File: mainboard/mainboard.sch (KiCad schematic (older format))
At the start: 29 parts, among them U1 ESP32-WROOM-32, U3 tps63070

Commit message: Add basic circuitry
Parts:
- added C12, C15, C18, C21, C24, C25, C3, C6, C9, C? (x10): C, symbol Device:C
- added C? (x2): 1 nC, symbol Device:C
- added D?: SP0503BAHT, Package_TO_SOT_SMD:SOT-143, symbol Power_Protection:SP0503BAHT
- added D?: D_Schottky, symbol Device:D_Schottky
- added J?: USB_B_Micro, symbol Connector:USB_B_Micro
- added J? (x2): Conn_01x19_MountingPin, symbol Connector_Generic_MountingPin:Conn_01x19_MountingPin
- added L3: L, symbol Device:L
- added Q?: PMV32UP, Package_TO_SOT_SMD:SOT-23, symbol pmv32up:PMV32UP
- added Q? (x2): Q_NPN_BCE, symbol Device:Q_NPN_BCE
- added R12, R13, R14, R3, R8, R9: R, symbol Device:R
- added R?: 4.7 kR, symbol Device:R
- added R? (x3): 470 R, symbol Device:R
- added R?: 100 kR, symbol Device:R
- added R?: 1 kR, symbol Device:R
- added R? (x2): 12 kR, symbol Device:R
- added SW? (x2): SW_Push, symbol Switch:SW_Push
- added U4: tps63070, tps63070:VQFN-HR-15, symbol tps63070:tps63070
- added U5: CP2102N-A01-GQFN24, Package_DFN_QFN:QFN-24-1EP_4x4mm_P0.5mm_EP2.6x2.6mm, symbol Interface_USB:CP2102N-A01-GQFN24
- gave numbers to parts that had none: 27
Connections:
- net labels added: D+, D-, DTR, EN, GSCLK, IO0, LAT, RTS, RXD, SCLK, SIN0, SOUT0, SOUT1, TXD, VBUS, VDC, VUSB, ~PG_VCC0, ~PG_VCC1
- net labels removed: +VDC, ~PG_VCC
- wire segments 144 -> 434
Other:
- note added: "balancing\nresistor"
- moved on the sheet: U1

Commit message: Add sensors
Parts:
- removed R13, R14: R, symbol Device:R
- added C?: 100 nC, Capacitor_SMD:C_0805_2012Metric, symbol Device:C
- added C?: 100 nC, symbol Device:C
- added C?: C, symbol Device:C
- added F? (x3): Fuse, symbol Device:Fuse
- added JP? (x2): Jumper_3_Bridged12, symbol Jumper:Jumper_3_Bridged12
- added U?: BME680, Package_LGA:Bosch_LGA-8_3x3mm_P0.8mm_ClockwisePinNumbering, symbol Sensor:BME680
- added U?: BH1750FVI, symbol BH1750:BH1750FVI
- C1, C16, C17, C18, C19, C2, C20, C21, C22, C23, C24, C25, C3, C4, C5, C6: footprint (none) -> Capacitor_SMD:C_0805_2012Metric
- C10, C11, C12: value C -> 100 nC; footprint (none) -> Capacitor_SMD:C_0805_2012Metric
- C13, C14, C15, C7, C8, C9: footprint (none) -> Capacitor_SMD:C_0603_1608Metric
- C26, C27, C28, C29, C30, C31, C32, C33, C34, C35, C36, C37: renamed from C?; footprint (none) -> Capacitor_SMD:C_0805_2012Metric
- J2, J3: renamed from J?; footprint (none) -> mainboard:Molex_Easy-On_52746-1971_1x19_P0.5mm_Horizontal
- L1, L2, L3: footprint (none) -> Inductor_SMD:L_Coilcraft_XxL4020
- R1, R10, R11, R12, R2, R3: value R -> 10 kR; footprint (none) -> Resistor_SMD:R_0805_2012Metric
- R15, R16, R17, R18, R19, R20, R21, R22: renamed from R?; footprint (none) -> Resistor_SMD:R_0805_2012Metric
- R4, R6, R8: value R -> 470 kR; footprint (none) -> Resistor_SMD:R_0805_2012Metric
- R5: value R -> 150 kR; footprint (none) -> Resistor_SMD:R_0805_2012Metric
- R7, R9: value R -> 120 kR; footprint (none) -> Resistor_SMD:R_0805_2012Metric
- gave numbers to parts that had none: 8
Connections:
- net labels added: PG_3V3, PG_VCC0, PG_VCC1, SCL, SDA, VCC_EAR0, VCC_EAR1
- net labels removed: VCC, ~PG_3V3, ~PG_VCC0, ~PG_VCC1
- wire segments 434 -> 478
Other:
- note added: "BOOT SELECT"
- note added: "EAR CONNECTORS"
- note added: "ENVIRON I2C"
- note added: "LED VCC"
- note added: "LUX I2C"
- note added: "POWER SELECT"
- note added: "USB <-> UART"
- note added: "VDD 3V3"
- note added: "WROOM32"
- note removed: "balancing\nresistor"
- moved on the sheet: C25, C26, C27, C28, C29, C30, C31, C32, C33, C34, C35, C36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

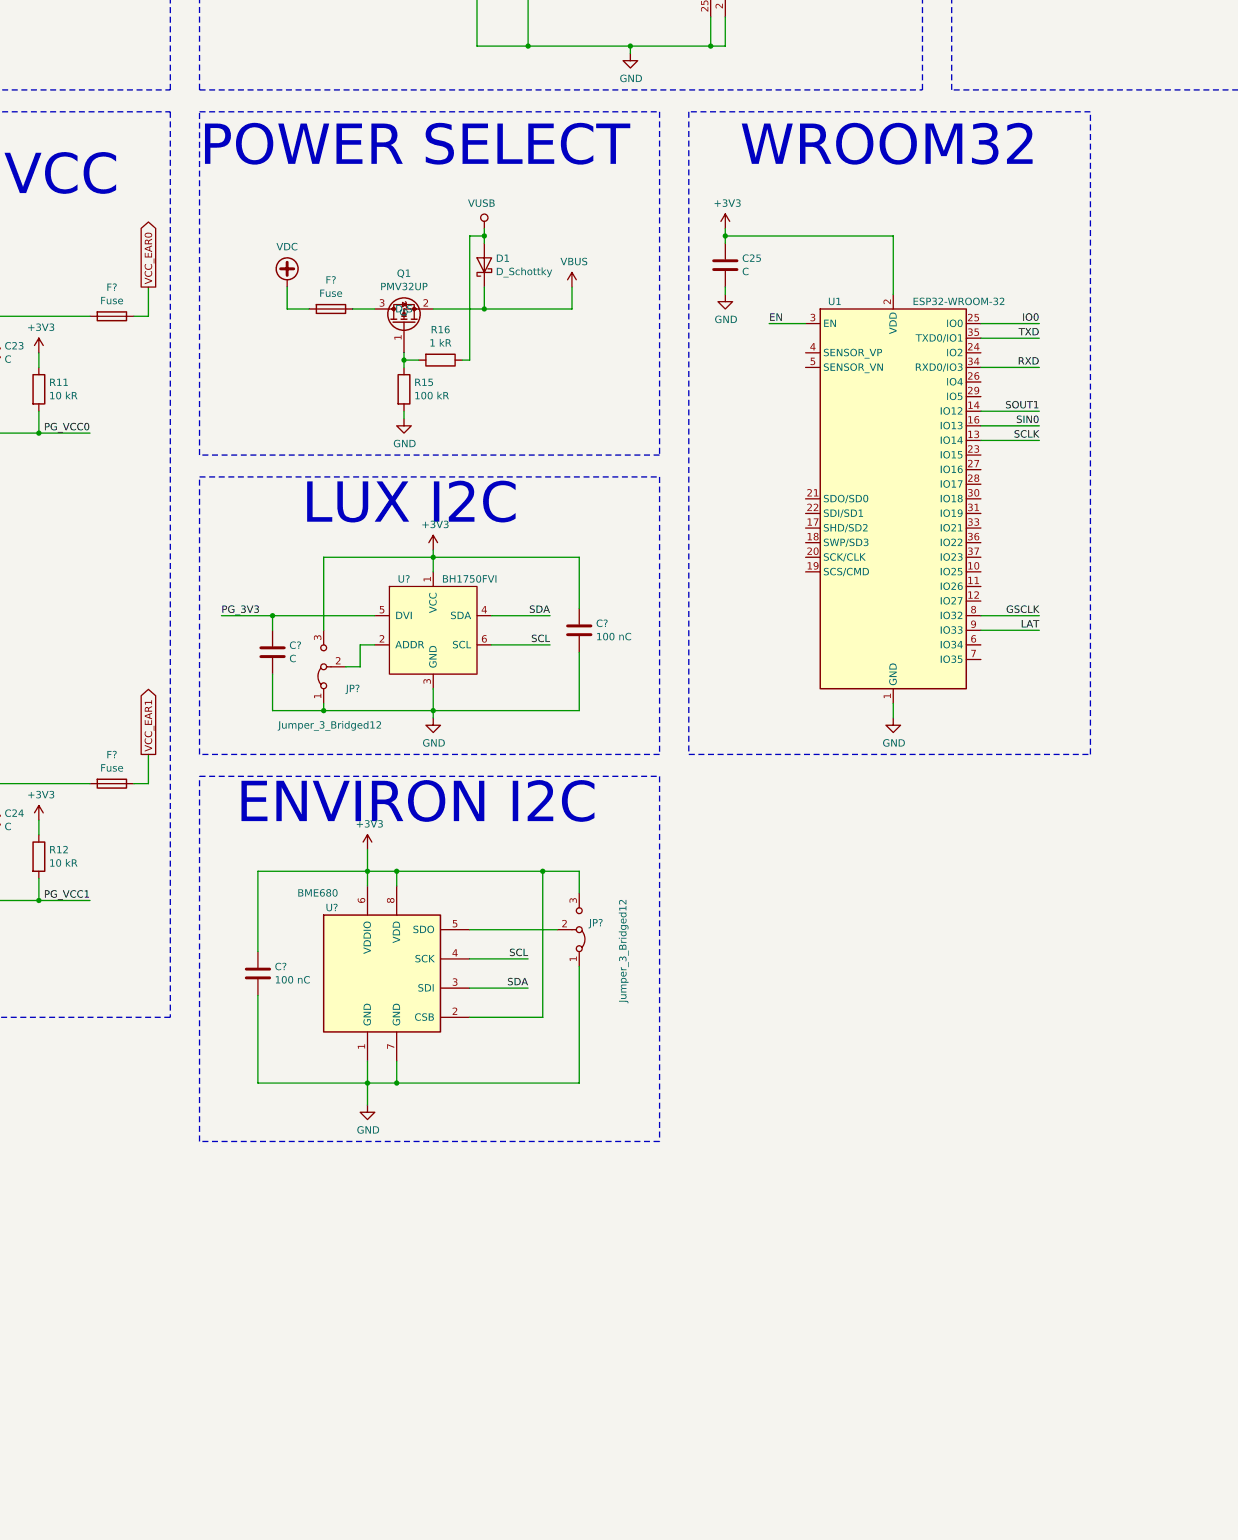
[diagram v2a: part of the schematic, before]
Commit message: Add accelerometer and magnetometer
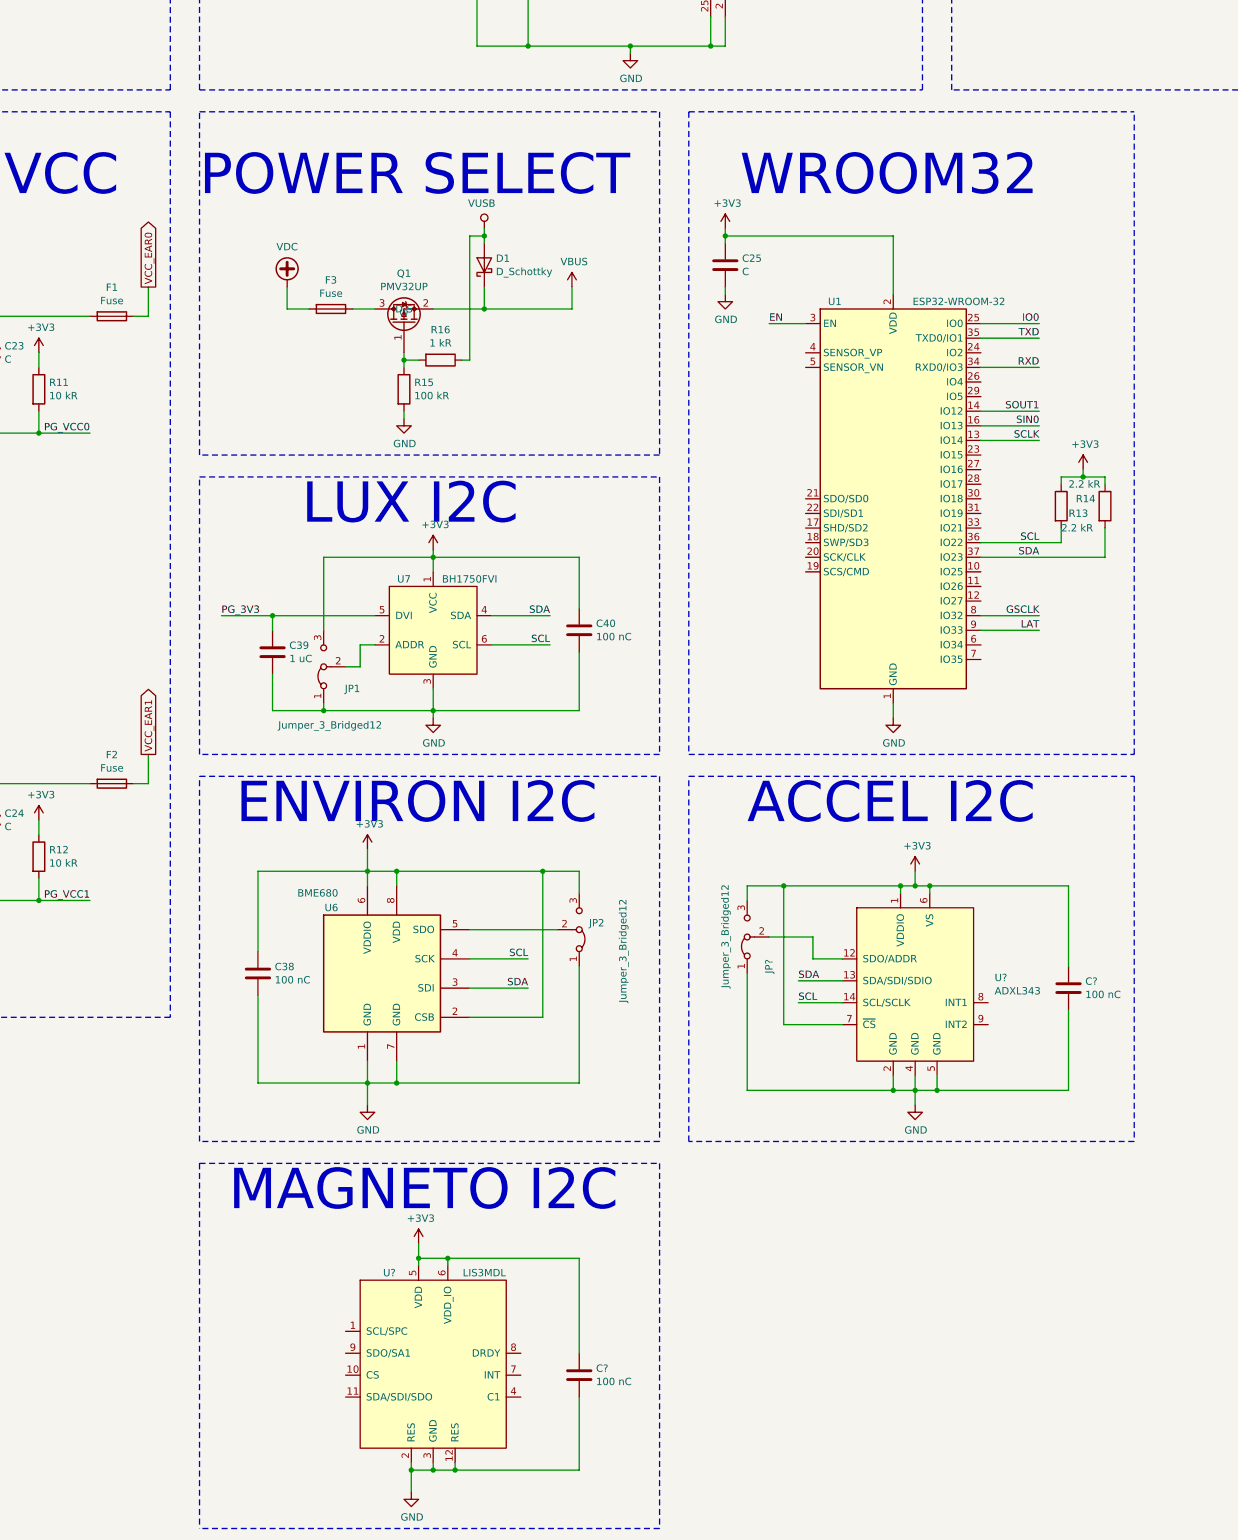
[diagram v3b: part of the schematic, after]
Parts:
- added C? (x2): 100 nC, symbol Device:C
- added JP?: Jumper_3_Bridged12, symbol Jumper:Jumper_3_Bridged12
- added R13, R14: 2.2 kR, symbol Device:R
- added U?: LIS3MDL, symbol LIS3MDL:LIS3MDL
- added U?: ADXL343, symbol ADXL343:ADXL343
- C39: renamed from C?; value C -> 1 uC
- gave numbers to parts that had none: 9
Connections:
- net +3V3: now also C?.1, C?.1, JP?.3 (B), R13.1, R14.1, U?.1 (VDDIO), U?.5 (VDD), U?.6 (VDD_IO), U?.6 (VS), U?.7 (~CS)
- net GND: now also C?.2, C?.2, JP?.1 (A), U?.12 (RES), U?.2 (GND), U?.2 (RES), U?.3 (GND), U?.4 (GND), U?.5 (GND)
- net SCL: now also U1.36 (IO22), R13.2, U?.14 (SCL/SCLK)
- net SDA: now also U1.37 (IO23), R14.2, U?.13 (SDA/SDI/SDIO)
- new net: JP?.2 (C), U?.12 (SDO/ADDR)
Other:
- note added: "ACCEL I2C"
- note added: "MAGNETO I2C"

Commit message: Layouting WIP
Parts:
- removed JP?: Jumper_3_Bridged12, symbol Jumper:Jumper_3_Bridged12
- removed Q1: PMV32UP, Package_TO_SOT_SMD:SOT-23, symbol pmv32up:PMV32UP
- removed Q2, Q3: Q_NPN_BCE, symbol Device:Q_NPN_BCE
- added C41: 100 nC, Capacitor_SMD:C_0805_2012Metric, symbol Device:C
- added JP3: Jumper_3_Bridged12, Jumper:SolderJumper-3_P1.3mm_Bridged12_Pad1.0x1.5mm, symbol Jumper:Jumper_3_Bridged12
- added JP4: Jumper, Jumper:SolderJumper-2_P1.3mm_Bridged_Pad1.0x1.5mm, symbol Device:Jumper
- added Q1: DMG2301L, Package_TO_SOT_SMD:SOT-23, symbol Transistor_FET:DMG2301L
- added Q2, Q3: MMBT3904, Package_TO_SOT_SMD:SOT-23, symbol Transistor_BJT:MMBT3904
- C39, C40: footprint (none) -> Capacitor_SMD:C_0805_2012Metric
- C42, C43: renamed from C?; footprint (none) -> Capacitor_SMD:C_0805_2012Metric
- D1: value D_Schottky -> PMEG3050EP,115; footprint (none) -> mainboard:SOD-128-2
- F1, F2, F3: footprint (none) -> Fuse:Fuse_0805_2012Metric
- J1: footprint (none) -> Connector_USB:USB_Micro-B_Amphenol_10103594-0001LF_Horizontal
- JP1, JP2: footprint (none) -> Jumper:SolderJumper-3_P1.3mm_Bridged12_Pad1.0x1.5mm
- R13, R14: footprint (none) -> Resistor_SMD:R_0805_2012Metric
- SW1, SW2: footprint (none) -> Button_Switch_SMD:SW_Push_SPST_NO_Alps_SKRK
- U7: footprint (none) -> mainboard:WSOF6I
- U8: renamed from U?; footprint (none) -> Package_LGA:LGA-12_2x2mm_P0.5mm
- U9: renamed from U?; footprint (none) -> Package_LGA:LGA-14_3x5mm_P0.8mm_LayoutBorder1x6y
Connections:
- net +3V3: now also U8.10 (CS), JP3.3 (B); no longer R11.1, R12.1, U9.7 (~CS)
- net DTR: now also Q3.2 (E)
- net EN: now also Q2.3 (C)
- net GND: now also R11.2, R12.2, C41.2, JP3.1 (A)
- net IO0: now also Q3.3 (C)
- net PG_VCC0: now also U1.27 (IO16); no longer R11.2
- net PG_VCC1: now also U1.28 (IO17); no longer R12.2
- net RTS: now also Q2.2 (E)
- net SCL: now also U1.10 (IO25), U8.1 (SCL/SPC); no longer U1.36 (IO22), U9.14 (SCL/SCLK)
- net SDA: now also U1.11 (IO26), U8.11 (SDA/SDI/SDO); no longer U1.37 (IO23), U9.13 (SDA/SDI/SDIO)
- net SOUT1: now also JP4.2; no longer U1.14 (IO12)
- net VBUS: now also Q1.2 (S); no longer C2.1, C3.1, C5.1, C6.1, C8.1, C9.1, R2.2, R3.2, U2.12 (VIN), U4.12 (VIN)
- net VDC: now also C2.1, C3.1, C5.1, C6.1, C8.1, C9.1, R2.2, R3.2, U2.12 (VIN), U4.12 (VIN)
- net VCC1_EN: now reaches U1.12 (IO27)
- net VCC1_EN: now also R12.1, U4.14 (EN)
- net SCK: now reaches U1.30 (IO18)
- net SCK: now also U9.14 (SCL/SCLK)
- net MISO: now reaches U1.31 (IO19)
- net MISO: now also U9.12 (SDO/ADDR)
- net ~CS_ACCEL: now reaches U1.33 (IO21)
- net ~CS_ACCEL: now also U9.7 (~CS)
- net DRDY: now reaches U1.4 (SENSOR_VP)
- net DRDY: now also U8.8 (DRDY)
- net INT: now reaches U1.5 (SENSOR_VN)
- net INT: now also U8.7 (INT)
- net INT1: now reaches U1.6 (IO34)
- net INT1: now also U9.8 (INT1)
- net INT2: now reaches U1.7 (IO35)
- net INT2: now also U9.9 (INT2)
- net at U8.4 (C1): now also C41.1
- net at U8.9 (SDO/SA1): now also JP3.2 (C)
- net at R15.1, R16.2: now also Q1.1 (G)
- net at F3.1: now also Q1.3 (D)
- net at R19.1: now also Q2.1 (B)
- net at R20.1: now also Q3.1 (B)
- net VCC_EN renamed VCC0_EN
- net VCC0_EN: now also R11.1, U1.36 (IO22); no longer U4.14 (EN)
- new net: JP4.1, U1.14 (IO12)
- new net MOSI: U1.37 (IO23), U9.13 (SDA/SDI/SDIO)
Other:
- note added: "ACCEL SPI"
- note removed: "ACCEL I2C"
- moved on the sheet: R13, R14

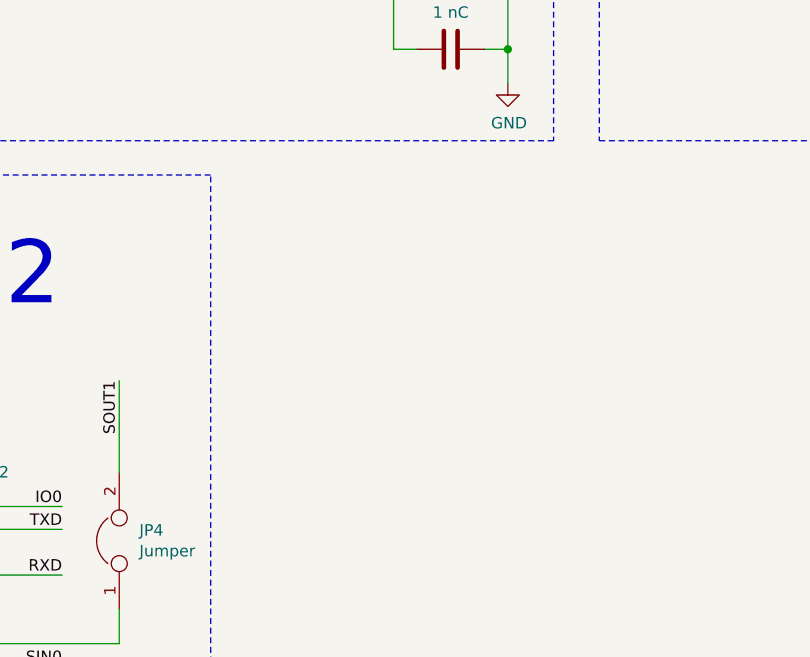
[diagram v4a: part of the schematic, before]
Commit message: Assemble regulator sections
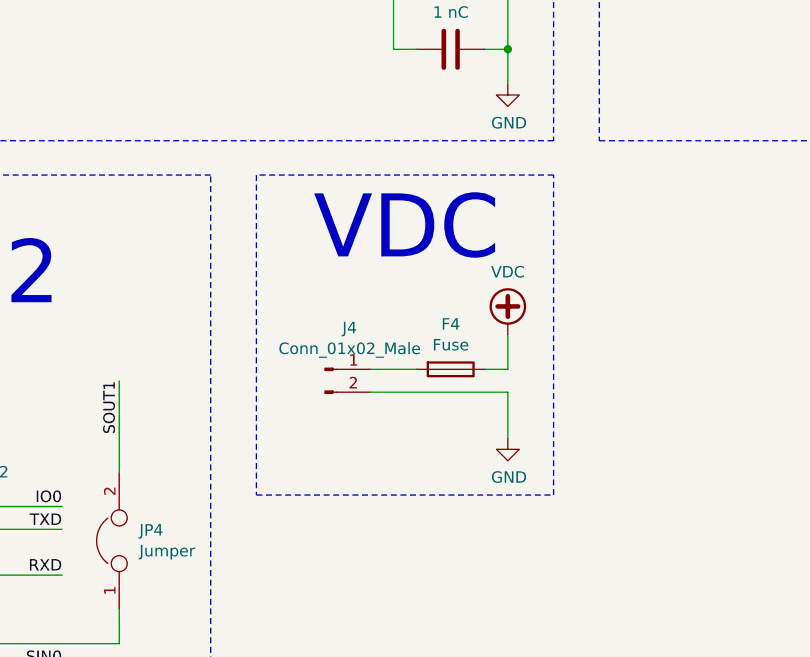
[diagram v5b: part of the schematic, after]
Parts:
- added F4: Fuse, Fuse:Fuse_0805_2012Metric, symbol Device:Fuse
- added J4: Conn_01x02_Male, symbol Connector:Conn_01x02_Male
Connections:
- net GND: now also J4.2 (Pin_2)
- net VDC: now also F4.1
- new net: F4.2, J4.1 (Pin_1)
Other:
- note added: "VDC"
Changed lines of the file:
@@
 $EndComp
 $Comp
-L power:VDC #PWR?
+L power:VDC #PWR0108
 U 1 1 5DDC5378
 P 850 4250
-F 0 "#PWR?" H 850 4150 50  0001 C CNN
+F 0 "#PWR0108" H 850 4150 50  0001 C CNN
 F 1 "VDC" H 850 4525 50  0000 C CNN
 F 2 "" H 850 4250 50  0001 C CNN
@@
 Wire Wire Line
 	850  4250 850  5300
-Wire Bus Line
-	8350 2150 8350 2500
-Wire Bus Line
-	9350 2500 9350 2750
 Connection ~ 850  5300
 $Comp
-L power:VDC #PWR?
+L power:VDC #PWR0116
 U 1 1 5DE58489
 P 850 7400
-F 0 "#PWR?" H 850 7300 50  0001 C CNN
+F 0 "#PWR0116" H 850 7300 50  0001 C CNN
 F 1 "VDC" H 850 7675 50  0000 C CNN
 F 2 "" H 850 7400 50  0001 C CNN
@@
 	1    0    0    -1
 $EndComp
+$Comp
+L power:VDC #PWR0117
+U 1 1 5DF194F2
+P 14550 4600
+F 0 "#PWR0117" H 14550 4500 50  0001 C CNN
+F 1 "VDC" H 14550 4875 50  0000 C CNN
+F 2 "" H 14550 4600 50  0001 C CNN
+F 3 "" H 14550 4600 50  0001 C CNN
+	1    14550 4600
+	1    0    0    -1
+$EndComp
+$Comp
+L Device:Fuse F4
+U 1 1 5DF1A160
+P 14300 4750
+F 0 "F4" V 14103 4750 50  0000 C CNN
+F 1 "Fuse" V 14194 4750 50  0000 C CNN
+F 2 "Fuse:Fuse_0805_2012Metric" V 14230 4750 50  0001 C CNN
+F 3 "~" H 14300 4750 50  0001 C CNN
+	1    14300 4750
+	0    1    1    0
+$EndComp
+Wire Wire Line
+	14450 4750 14550 4750
+Wire Wire Line
+	14550 4750 14550 4600
+$Comp
+L Connector:Conn_01x02_Male J4
+U 1 1 5DFAE882
+P 13750 4750
+F 0 "J4" H 13858 4931 50  0000 C CNN
+F 1 "Conn_01x02_Male" H 13858 4840 50  0000 C CNN
+F 2 "" H 13750 4750 50  0001 C CNN
+F 3 "~" H 13750 4750 50  0001 C CNN
+	1    13750 4750
+	1    0    0    -1
+$EndComp
+Wire Wire Line
+	13950 4750 14150 4750
+$Comp
+L power:GND #PWR0124
+U 1 1 5DFF9B28
+P 14550 5050
+F 0 "#PWR0124" H 14550 4800 50  0001 C CNN
+F 1 "GND" H 14555 4877 50  0000 C CNN
+F 2 "" H 14550 5050 50  0001 C CNN
+F 3 "" H 14550 5050 50  0001 C CNN
+	1    14550 5050
+	1    0    0    -1
+$EndComp
+Wire Wire Line
+	14550 5050 14550 4850
+Wire Wire Line
+	14550 4850 13950 4850
+Wire Notes Line
+	13450 3900 13450 5300
+Wire Notes Line
+	13450 5300 14750 5300
+Wire Notes Line
+	14750 5300 14750 3900
+Wire Notes Line
+	14750 3900 13450 3900
+Text Notes 13700 4300 0    276  ~ 0
+VDC
+Wire Bus Line
+	8350 2150 8350 2500
+Wire Bus Line
+	9350 2500 9350 2750
 $EndSCHEMATC
